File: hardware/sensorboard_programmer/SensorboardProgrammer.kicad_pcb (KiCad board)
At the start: 2 copper layers, 21.8 x 17.8 mm, 4 parts

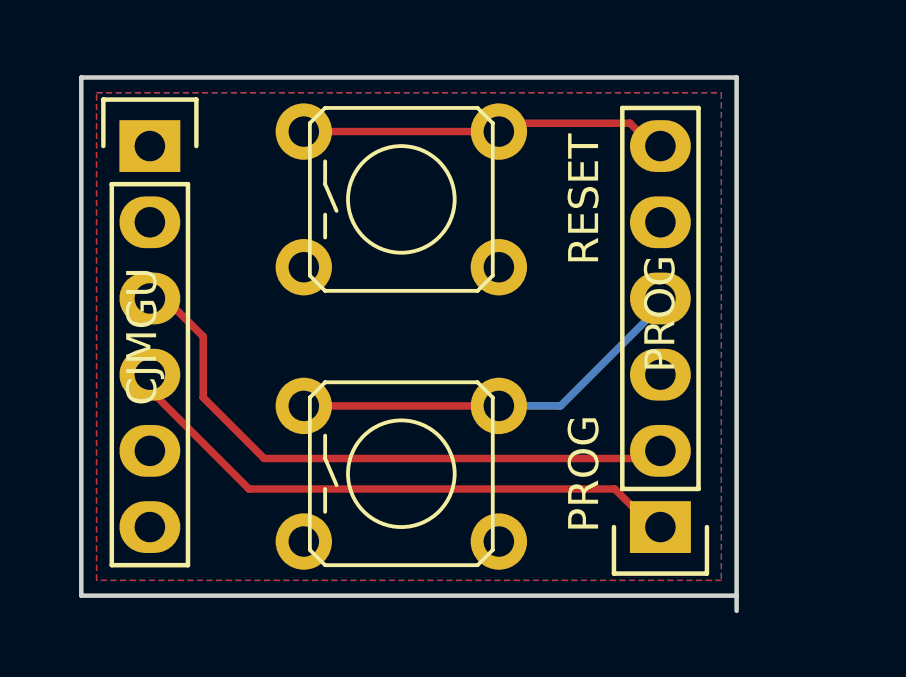
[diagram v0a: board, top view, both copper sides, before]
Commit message: Better silkscreening and status LEDs.
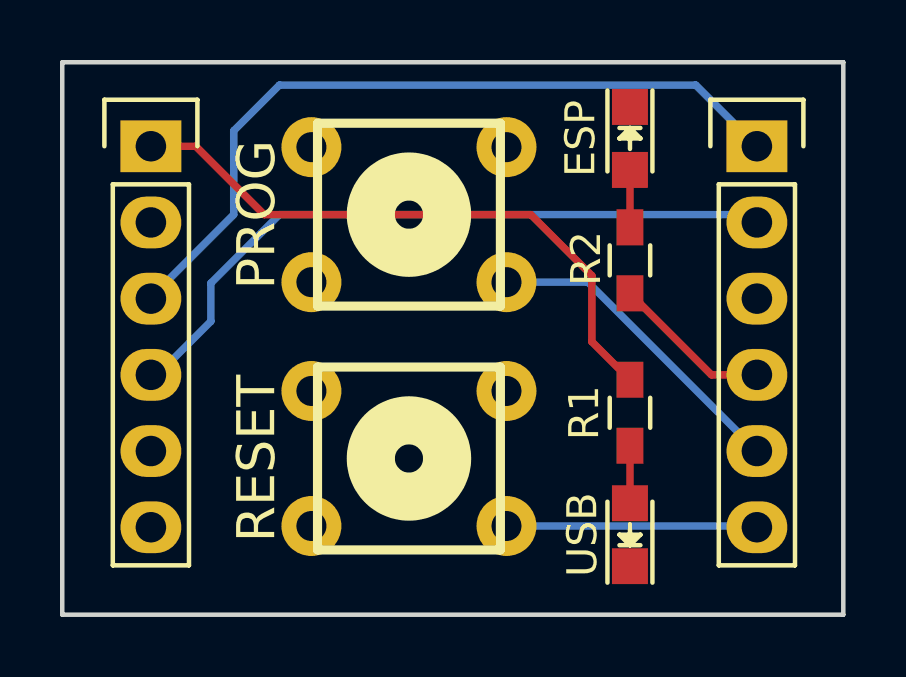
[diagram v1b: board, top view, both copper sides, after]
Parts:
- removed CJMGU: CONN_01X06, Pin_Headers:Pin_Header_Straight_1x06
- removed the PROG at (151.4, 53.6)
- removed the PROG at (142.7, 51.8)
- removed the RESET at (142.7, 42.7)
- added ESP: ESP, LEDs:LED-0805, F.Cu at (150.4, 40.6)
- added P2: CONN_01X06, Pin_Headers:Pin_Header_Straight_1x06, F.Cu at (154.6, 40.9)
- added PROG: SW_PUSH, w_switch:PCB_PUSH, F.Cu at (143.0, 43.2)
- added R1: 100 ohm, Resistors_SMD:R_0603_HandSoldering, F.Cu at (150.4, 49.8)
- added R2: 100 ohm, Resistors_SMD:R_0603_HandSoldering, F.Cu at (150.4, 44.7)
- added RESET: SW_PUSH, w_switch:PCB_PUSH, F.Cu at (143.0, 51.3)
- added USB: USB, LEDs:LED-0805, F.Cu at (150.4, 53.8)
- added USB MODULE: CONN_01X06, Pin_Headers:Pin_Header_Straight_1x06, F.Cu at (134.4, 40.9)
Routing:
- net Net-(P1-Pad1): track 0.00 -> 20.5 mm
- net Net-(P2-Pad5): track 0.00 -> 10.7 mm
- net Net-(P2-Pad4): track 13.3 -> 5.36 mm
- net RXI: track 20.4 -> 25.7 mm
- net TXO: track 19.5 -> 23.3 mm
- net Net-(P2-Pad6): track 12.4 -> 8.77 mm
- net Net-(D2-Pad2): track 0.00 -> 1.91 mm
- net Net-(D1-Pad2): track 0.00 -> 1.91 mm
- added copper zone on F.Cu, net GND
- removed copper zone on F.Cu, net +3V3
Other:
- board size 21.8 x 17.8 mm -> 26 x 18.4 mm
- board text added: "3v3"
- board text added: "GND"
- board text added: "PRG"
- board text added: "RST"
- board text added: "RXI"
- board text added: "TXO"
